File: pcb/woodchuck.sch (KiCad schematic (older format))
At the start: 0 parts

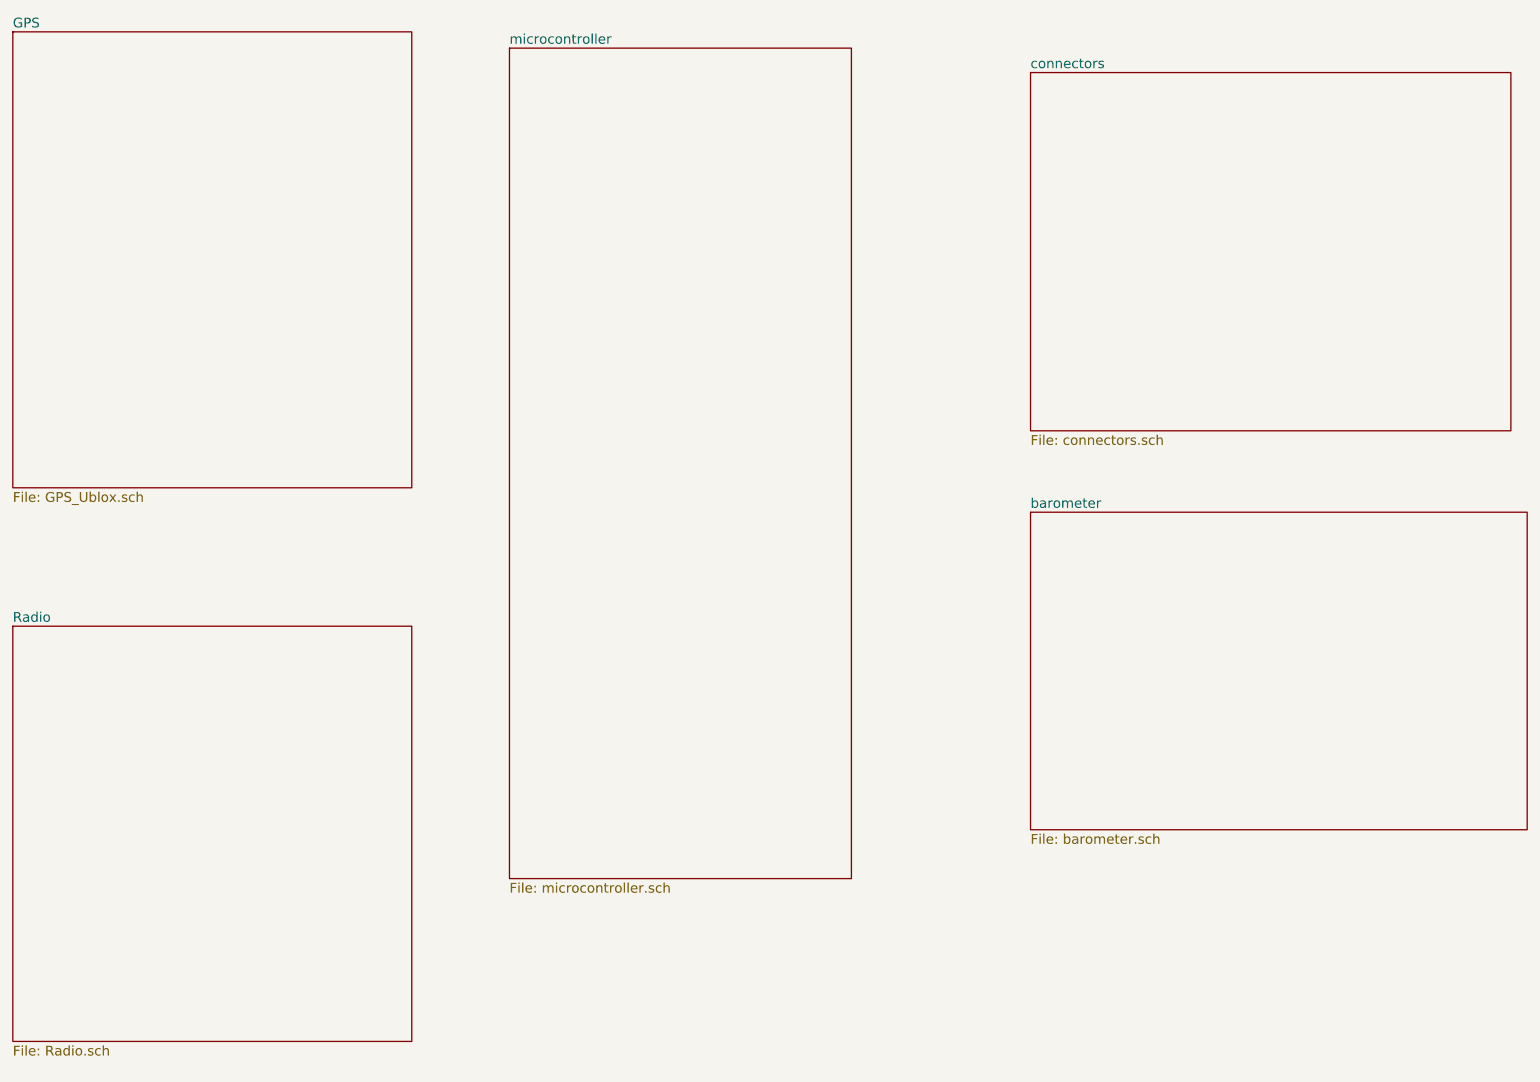
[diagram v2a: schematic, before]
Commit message: Add MTX2 circuit and add a sheet for power supply/regulation
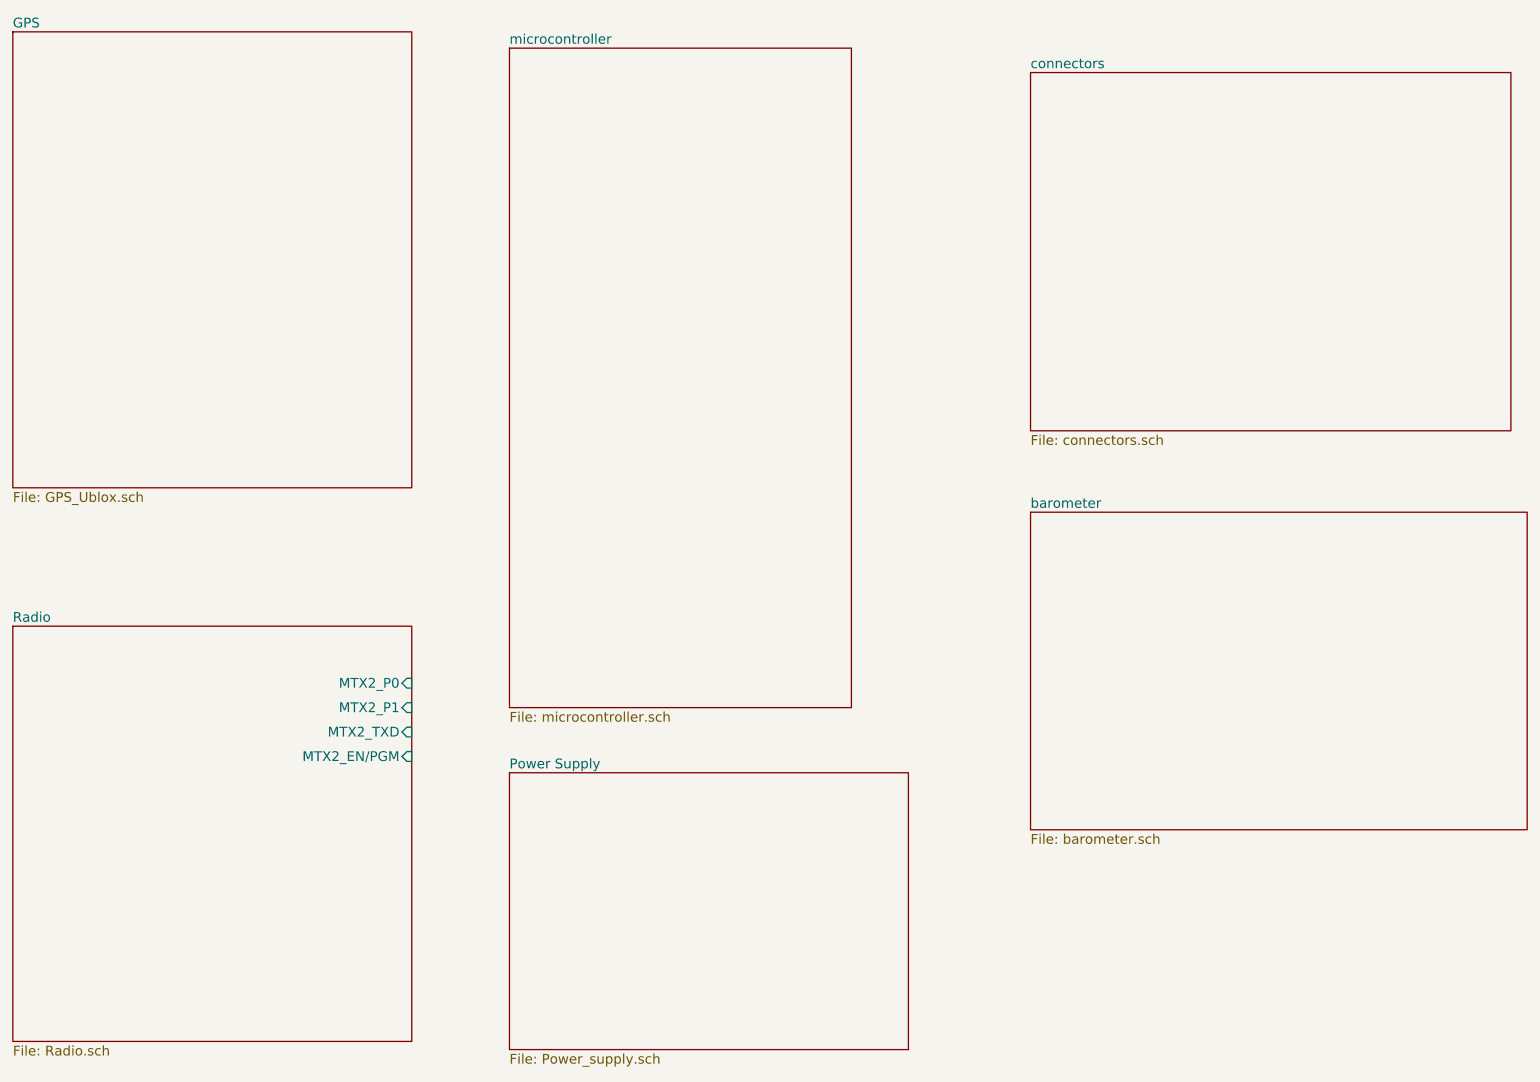
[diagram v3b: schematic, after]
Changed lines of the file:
@@
 LIBS:max-7q
 LIBS:ms5611-01ba03
-LIBS:quarter_wave_ant
 LIBS:resistor
 LIBS:rfm69w
-LIBS:sma
 LIBS:stm32f405vgt
 LIBS:swd
@@
 LIBS:stm32f072cbt6
 LIBS:jsta
+LIBS:sma
+LIBS:cga0402mlc-12g
 LIBS:woodchuck-cache
 EELAYER 25 0
@@
 $Descr A4 11693 8268
 encoding utf-8
-Sheet 1 6
+Sheet 1 7
 Title ""
 Date ""
@@
 F0 "Radio" 60
 F1 "Radio.sch" 60
+F2 "MTX2_P0" I R 3600 5050 60
+F3 "MTX2_P1" I R 3600 5200 60
+F4 "MTX2_TXD" I R 3600 5350 60
+F5 "MTX2_EN/PGM" I R 3600 5500 60
 $EndSheet
 $Sheet
-S 4200 1150 2100 5100
+S 4200 1150 2100 4050
 U 56574098
 F0 "microcontroller" 60
@@
 F1 "barometer.sch" 60
 $EndSheet
+$Sheet
+S 4200 5600 2450 1700
+U 565D06C2
+F0 "Power Supply" 60
+F1 "Power_supply.sch" 60
+$EndSheet
 $EndSCHEMATC

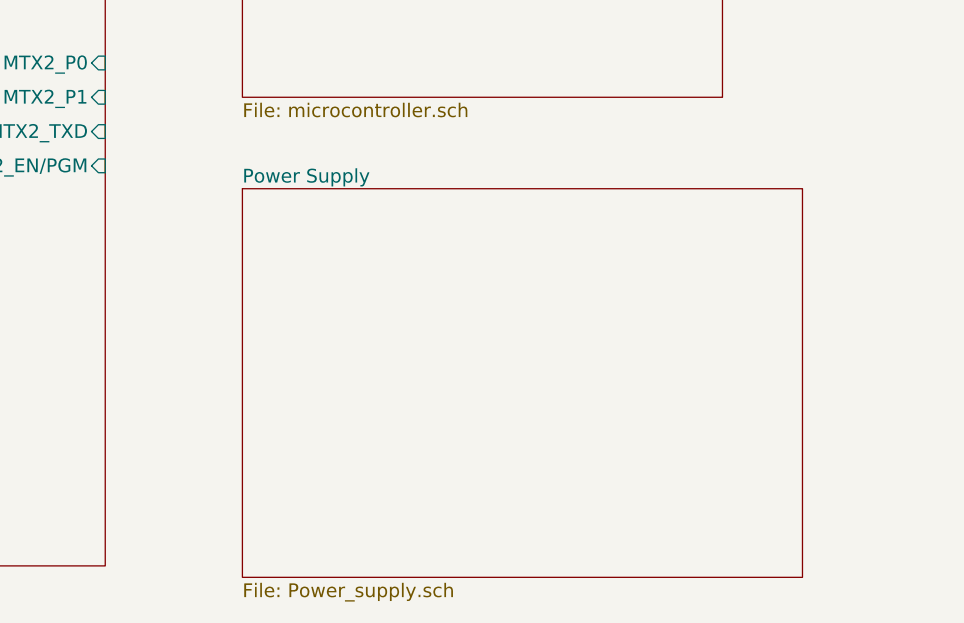
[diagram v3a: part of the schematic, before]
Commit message: Added power regulation. Using component ADP3335 as used in Avionics14.
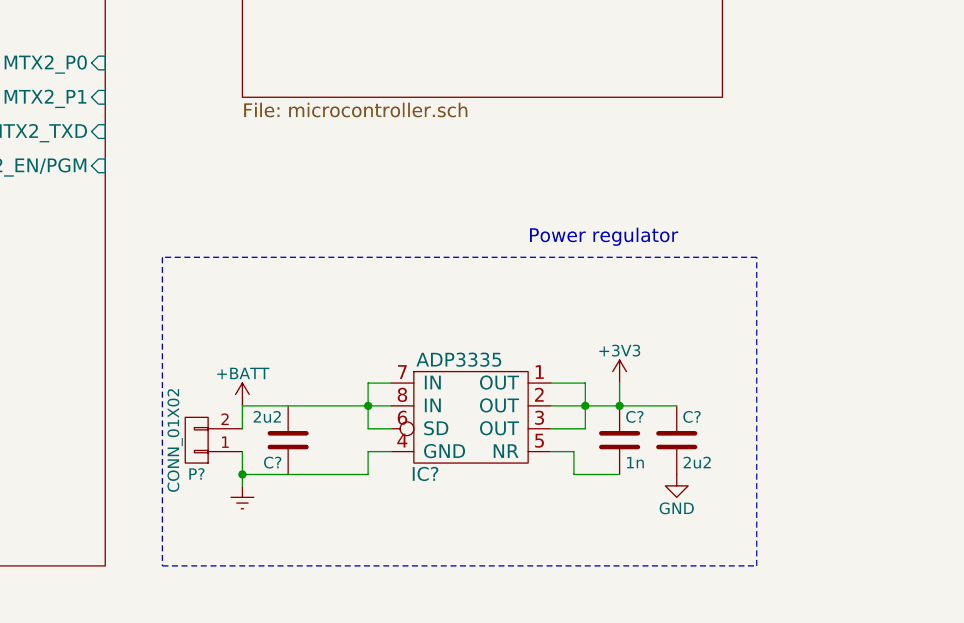
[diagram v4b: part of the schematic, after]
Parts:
- added C? (x2): 2u2, symbol C
- added C?: 1n, symbol C
- added IC?: ADP3335, symbol ADP3335
- added P?: CONN_01X02, symbol CONN_01X02
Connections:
- new net: C?.2, IC?.5 (NR)
- new net +3V3: C?.1, C?.1, IC?.1 (OUT), IC?.2 (OUT), IC?.3 (OUT)
- new net +BATT: IC?.6 (SD), IC?.7 (IN), IC?.8 (IN), P?.2 (P2)
- new net Earth: IC?.4 (GND), P?.1 (P1)
- new net GND: C?.2
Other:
- note added: "Power regulator"
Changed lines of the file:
@@
 $Descr A4 11693 8268
 encoding utf-8
-Sheet 1 7
+Sheet 1 6
 Title ""
 Date ""
@@
 F1 "barometer.sch" 60
 $EndSheet
-$Sheet
-S 4200 5600 2450 1700
-U 565D06C2
-F0 "Power Supply" 60
-F1 "Power_supply.sch" 60
-$EndSheet
+$Comp
+L ADP3335 IC?
+U 1 1 565E3BA6
+P 5200 6550
+F 0 "IC?" H 5000 6250 60  0000 C CNN
+F 1 "ADP3335" H 5150 6750 60  0000 C CNN
+F 2 "" H 5600 6150 60  0000 C CNN
+F 3 "" H 5600 6150 60  0000 C CNN
+	1    5200 6550
+	1    0    0    -1
+$EndComp
+Text Notes 5450 5850 0    60   ~ 0
+Power regulator
+$Comp
+L C C?
+U 1 1 565E4A3A
+P 5850 6700
+F 0 "C?" H 5875 6800 50  0000 L CNN
+F 1 "1n" H 5875 6600 50  0000 L CNN
+F 2 "" H 5888 6550 30  0000 C CNN
+F 3 "" H 5850 6700 60  0000 C CNN
+	1    5850 6700
+	1    0    0    -1
+$EndComp
+$Comp
+L Earth #PWR?
+U 1 1 565E4C8C
+P 4200 6900
+F 0 "#PWR?" H 4200 6650 50  0001 C CNN
+F 1 "Earth" H 4200 6750 50  0001 C CNN
+F 2 "" H 4200 6900 60  0000 C CNN
+F 3 "" H 4200 6900 60  0000 C CNN
+	1    4200 6900
+	1    0    0    -1
+$EndComp
+$Comp
+L C C?
+U 1 1 565E50FD
+P 6100 6700
+F 0 "C?" H 6125 6800 50  0000 L CNN
+F 1 "2u2" H 6125 6600 50  0000 L CNN
+F 2 "" H 6138 6550 30  0000 C CNN
+F 3 "" H 6100 6700 60  0000 C CNN
+	1    6100 6700
+	1    0    0    -1
+$EndComp
+Wire Notes Line
+	3850 7250 6450 7250
+Wire Notes Line
+	6450 7250 6450 5900
+Wire Notes Line
+	6450 5900 3850 5900
+Wire Wire Line
+	4200 6550 4850 6550
+Wire Notes Line
+	3850 5900 3850 7250
+Wire Wire Line
+	5550 6450 5700 6450
+Wire Wire Line
+	5700 6450 5700 6650
+Wire Wire Line
+	5700 6650 5550 6650
+Connection ~ 5700 6550
+Wire Wire Line
+	5550 6750 5650 6750
+Wire Wire Line
+	5650 6750 5650 6850
+Wire Wire Line
+	5650 6850 5850 6850
+Connection ~ 5850 6550
+Wire Wire Line
+	4850 6750 4750 6750
+Wire Wire Line
+	4750 6750 4750 6850
+Wire Wire Line
+	4750 6850 4200 6850
+Wire Wire Line
+	5850 6550 5850 6450
+Wire Wire Line
+	5550 6550 6100 6550
+Wire Wire Line
+	4750 6650 4850 6650
+Wire Wire Line
+	4750 6450 4750 6650
+Connection ~ 4750 6550
+$Comp
+L GND #PWR?
+U 1 1 565E565A
+P 6100 6850
+F 0 "#PWR?" H 6100 6600 50  0001 C CNN
+F 1 "GND" H 6100 6700 50  0000 C CNN
+F 2 "" H 6100 6850 60  0000 C CNN
+F 3 "" H 6100 6850 60  0000 C CNN
+	1    6100 6850
+	1    0    0    -1
+$EndComp
+$Comp
+L C C?
+U 1 1 565E43E2
+P 4400 6700
+F 0 "C?" H 4425 6800 50  0000 L CNN
+F 1 "2u2" H 4425 6600 50  0000 L CNN
+F 2 "" H 4438 6550 30  0000 C CNN
+F 3 "" H 4400 6700 60  0000 C CNN
+	1    4400 6700
+	-1   0    0    1
+$EndComp
+$Comp
+L CONN_01X02 P?
+U 1 1 565EBDD9
+P 4000 6700
+F 0 "P?" H 4000 6850 50  0000 C CNN
+F 1 "CONN_01X02" V 4100 6700 50  0000 C CNN
+F 2 "" H 4000 6700 60  0000 C CNN
+F 3 "" H 4000 6700 60  0000 C CNN
+	1    4000 6700
+	-1   0    0    1
+$EndComp
+Wire Wire Line
+	4200 6750 4200 6900
+Wire Wire Line
+	4200 6650 4200 6550
+$Comp
+L +BATT #PWR?
+U 1 1 565EBEEE
+P 4200 6550
+F 0 "#PWR?" H 4200 6400 50  0001 C CNN
+F 1 "+BATT" H 4200 6690 50  0000 C CNN
+F 2 "" H 4200 6550 60  0000 C CNN
+F 3 "" H 4200 6550 60  0000 C CNN
+	1    4200 6550
+	1    0    0    -1
+$EndComp
+Wire Wire Line
+	4750 6450 4850 6450
+Connection ~ 4200 6850
+$Comp
+L +3V3 #PWR?
+U 1 1 565EC163
+P 5850 6450
+F 0 "#PWR?" H 5850 6300 50  0001 C CNN
+F 1 "+3V3" H 5850 6590 50  0000 C CNN
+F 2 "" H 5850 6450 60  0000 C CNN
+F 3 "" H 5850 6450 60  0000 C CNN
+	1    5850 6450
+	1    0    0    -1
+$EndComp
 $EndSCHEMATC

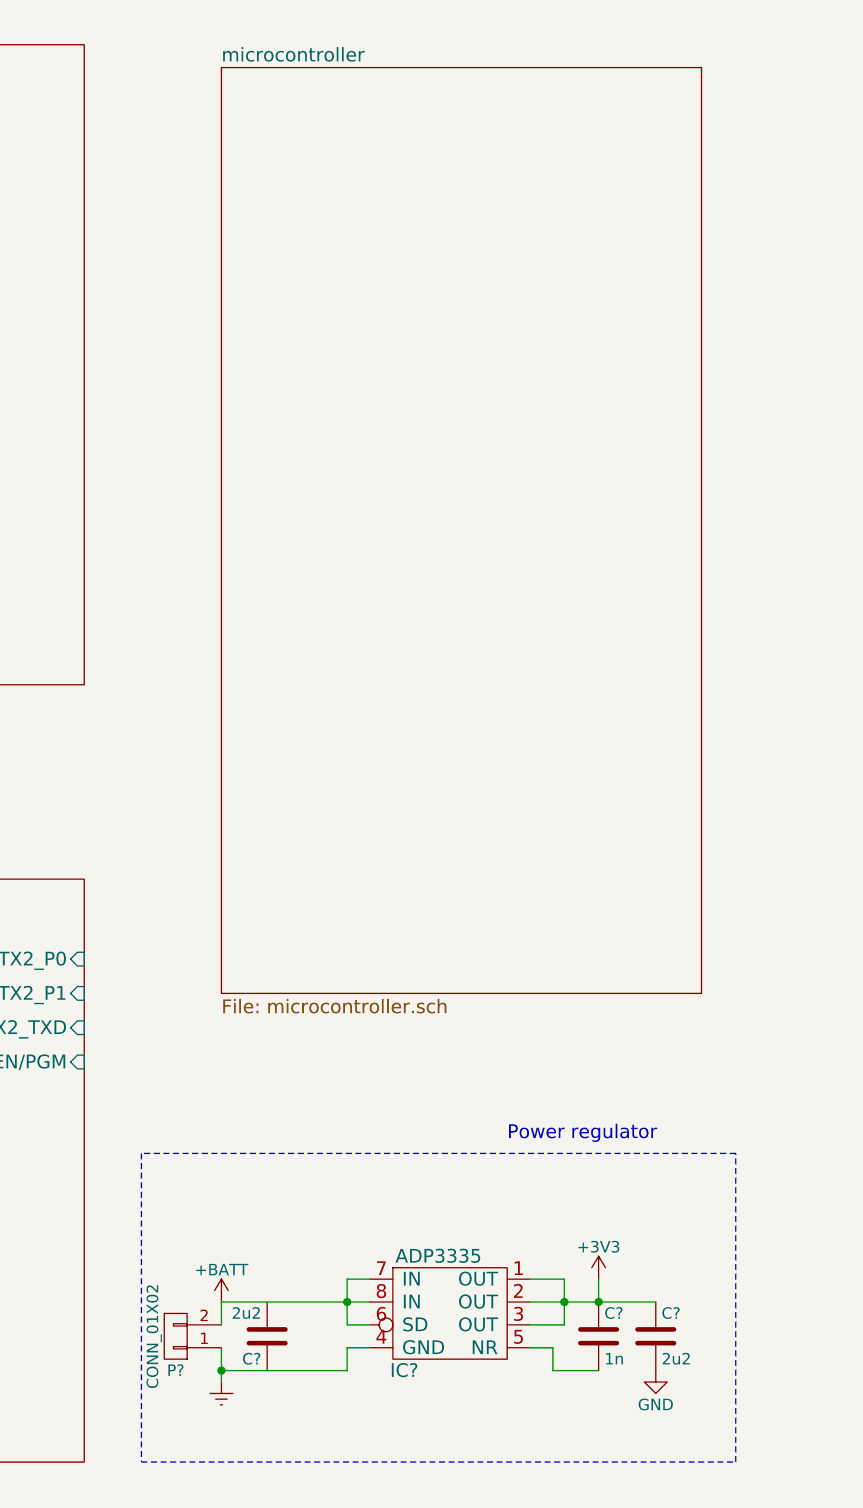
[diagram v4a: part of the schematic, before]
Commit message: Modify pin assignments of MCU
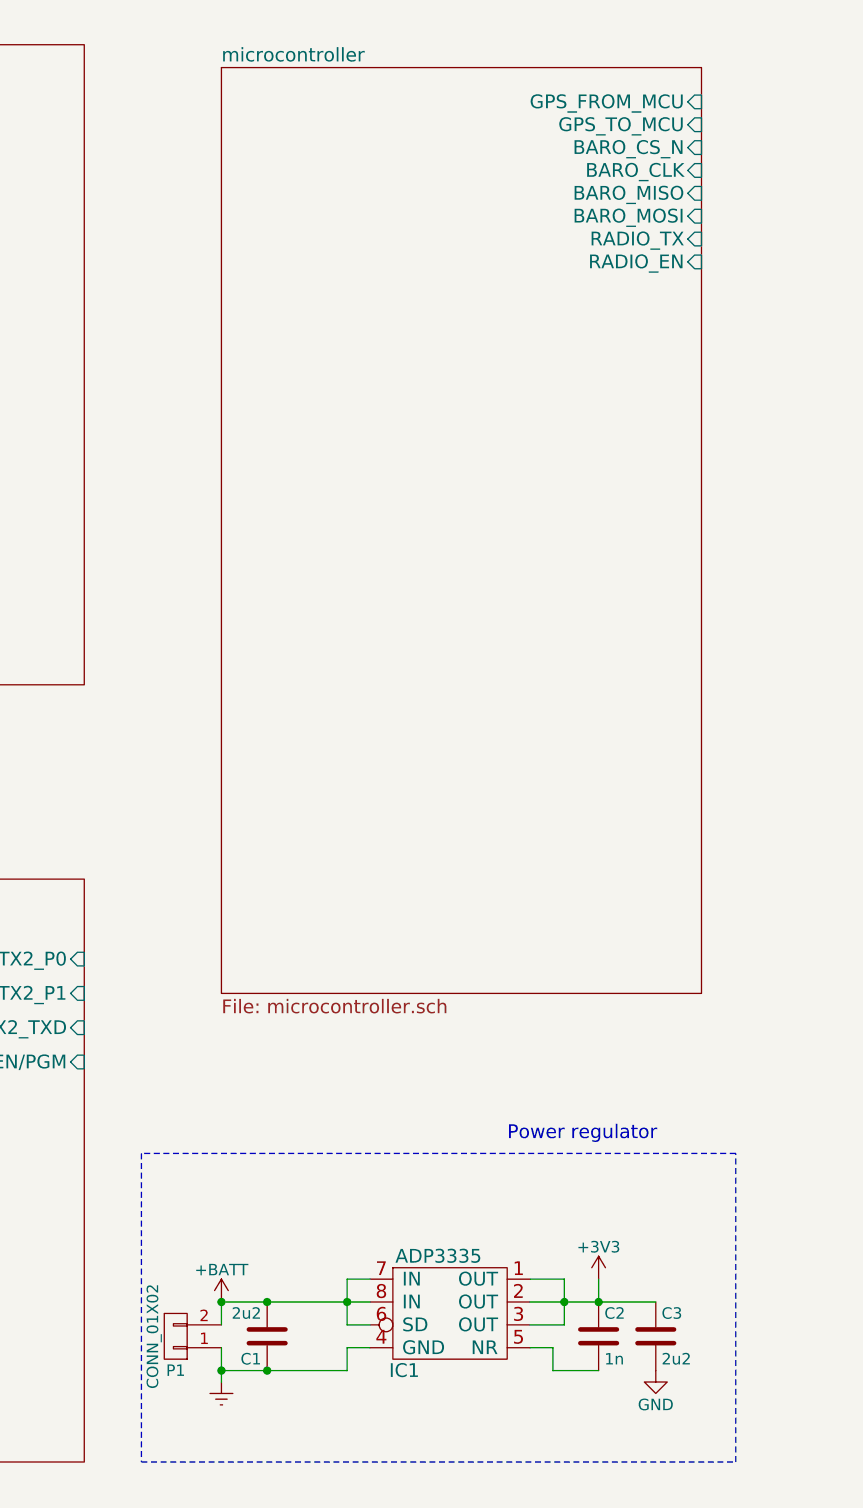
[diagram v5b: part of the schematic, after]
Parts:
- gave numbers to parts that had none: 5
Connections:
- net +BATT: now also C1.2
- net Earth: now also C1.1
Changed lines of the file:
@@
 F0 "microcontroller" 60
 F1 "microcontroller.sch" 60
+F2 "GPS_FROM_MCU" I R 6300 1300 60
+F3 "GPS_TO_MCU" I R 6300 1400 60
+F4 "BARO_CS_N" I R 6300 1500 60
+F5 "BARO_CLK" I R 6300 1600 60
+F6 "BARO_MISO" I R 6300 1700 60
+F7 "BARO_MOSI" I R 6300 1800 60
+F8 "RADIO_TX" I R 6300 1900 60
+F9 "RADIO_EN" I R 6300 2000 60
 $EndSheet
 $Sheet
@@
 $EndSheet
 $Comp
-L ADP3335 IC?
+L ADP3335 IC1
 U 1 1 565E3BA6
 P 5200 6550
-F 0 "IC?" H 5000 6250 60  0000 C CNN
+F 0 "IC1" H 5000 6250 60  0000 C CNN
 F 1 "ADP3335" H 5150 6750 60  0000 C CNN
 F 2 "" H 5600 6150 60  0000 C CNN
@@
 Power regulator
 $Comp
-L C C?
+L C C2
 U 1 1 565E4A3A
 P 5850 6700
-F 0 "C?" H 5875 6800 50  0000 L CNN
+F 0 "C2" H 5875 6800 50  0000 L CNN
 F 1 "1n" H 5875 6600 50  0000 L CNN
 F 2 "" H 5888 6550 30  0000 C CNN
@@
 $EndComp
 $Comp
-L Earth #PWR?
+L Earth #PWR01
 U 1 1 565E4C8C
 P 4200 6900
-F 0 "#PWR?" H 4200 6650 50  0001 C CNN
+F 0 "#PWR01" H 4200 6650 50  0001 C CNN
 F 1 "Earth" H 4200 6750 50  0001 C CNN
 F 2 "" H 4200 6900 60  0000 C CNN
@@
 $EndComp
 $Comp
-L C C?
+L C C3
 U 1 1 565E50FD
 P 6100 6700
-F 0 "C?" H 6125 6800 50  0000 L CNN
+F 0 "C3" H 6125 6800 50  0000 L CNN
 F 1 "2u2" H 6125 6600 50  0000 L CNN
 F 2 "" H 6138 6550 30  0000 C CNN
@@
 Connection ~ 4750 6550
 $Comp
-L GND #PWR?
+L GND #PWR02
 U 1 1 565E565A
 P 6100 6850
-F 0 "#PWR?" H 6100 6600 50  0001 C CNN
+F 0 "#PWR02" H 6100 6600 50  0001 C CNN
 F 1 "GND" H 6100 6700 50  0000 C CNN
 F 2 "" H 6100 6850 60  0000 C CNN
@@
 $EndComp
 $Comp
-L C C?
+L C C1
 U 1 1 565E43E2
 P 4400 6700
-F 0 "C?" H 4425 6800 50  0000 L CNN
+F 0 "C1" H 4425 6800 50  0000 L CNN
 F 1 "2u2" H 4425 6600 50  0000 L CNN
 F 2 "" H 4438 6550 30  0000 C CNN
@@
 $EndComp
 $Comp
-L CONN_01X02 P?
+L CONN_01X02 P1
 U 1 1 565EBDD9
 P 4000 6700
-F 0 "P?" H 4000 6850 50  0000 C CNN
+F 0 "P1" H 4000 6850 50  0000 C CNN
 F 1 "CONN_01X02" V 4100 6700 50  0000 C CNN
 F 2 "" H 4000 6700 60  0000 C CNN
@@
 	4200 6650 4200 6550
 $Comp
-L +BATT #PWR?
+L +BATT #PWR03
 U 1 1 565EBEEE
 P 4200 6550
-F 0 "#PWR?" H 4200 6400 50  0001 C CNN
+F 0 "#PWR03" H 4200 6400 50  0001 C CNN
 F 1 "+BATT" H 4200 6690 50  0000 C CNN
 F 2 "" H 4200 6550 60  0000 C CNN
@@
 Connection ~ 4200 6850
 $Comp
-L +3V3 #PWR?
+L +3V3 #PWR04
 U 1 1 565EC163
 P 5850 6450
-F 0 "#PWR?" H 5850 6300 50  0001 C CNN
+F 0 "#PWR04" H 5850 6300 50  0001 C CNN
 F 1 "+3V3" H 5850 6590 50  0000 C CNN
 F 2 "" H 5850 6450 60  0000 C CNN
@@
 	1    0    0    -1
 $EndComp
+Connection ~ 4400 6850
+Connection ~ 4400 6550
+Connection ~ 4200 6550
 $EndSCHEMATC
